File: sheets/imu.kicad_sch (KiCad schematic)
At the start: 11 parts, among them CN1 StemmaQT, CN2 StemmaQT, U2 BMP581, U5 ADXL375BCCZ-RL7, U7 ADXL345BCCZ-RL7

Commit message: added current rush limiting resistors to bmp581
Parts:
- added R24, R25: 10, symbol Device:R
- U5: footprint easyeda2kicad:LGA-14_L5.0-W3.0-P0.80-BL -> aerolotl_custom:LGA-14_L5.0-W3.0-P0.80-BL
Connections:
- net GND: now also CIO1.2, CS1.2, U5.11 (RESERVED), U7.11 (RESERVED_11)
- net VDD: now also U5.3 (RESERVED), U7.3 (RESERVED_3), R24.1, R25.1; no longer C32.1, C33.1, U2.1 (VDDIO), U2.10 (VDD)
- net ADXL345.INT: now reaches U7.8 (INT1)
- net ADXL375.INT: now reaches U5.8 (INT1)
- new net: C32.1, R24.2, U2.10 (VDD)
- new net: C33.1, R25.2, U2.1 (VDDIO)
- no-connect marks 2 -> 4
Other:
- note added: "ADXL375"
- note added: "BNO085 uses the Adafruit breakout board (no chip in stock in JLCPCB) via a StemmaQT connector"
- note added: "NEOM9N uses sparkfun breakout board"
- note added: "R = 10Ohm for inrush current limiting + LPF for stable voltage source"
- note removed: "TODO list: - Add the stemma qt adapter for the BNO085 -> DONE (Only labeled; from FlyPho) - Add the BMP581 connections (SPI 4-wire) -> DONE (from datasheet) - Add UART to GPS Neo m9n module -> WAITING (possible ITAR restriction) - Add ADXL345 and ADXL 375 via SPI -> IN PROGRESS"
- moved on the sheet: C32, C33, CIO1, CS1, U2, U5

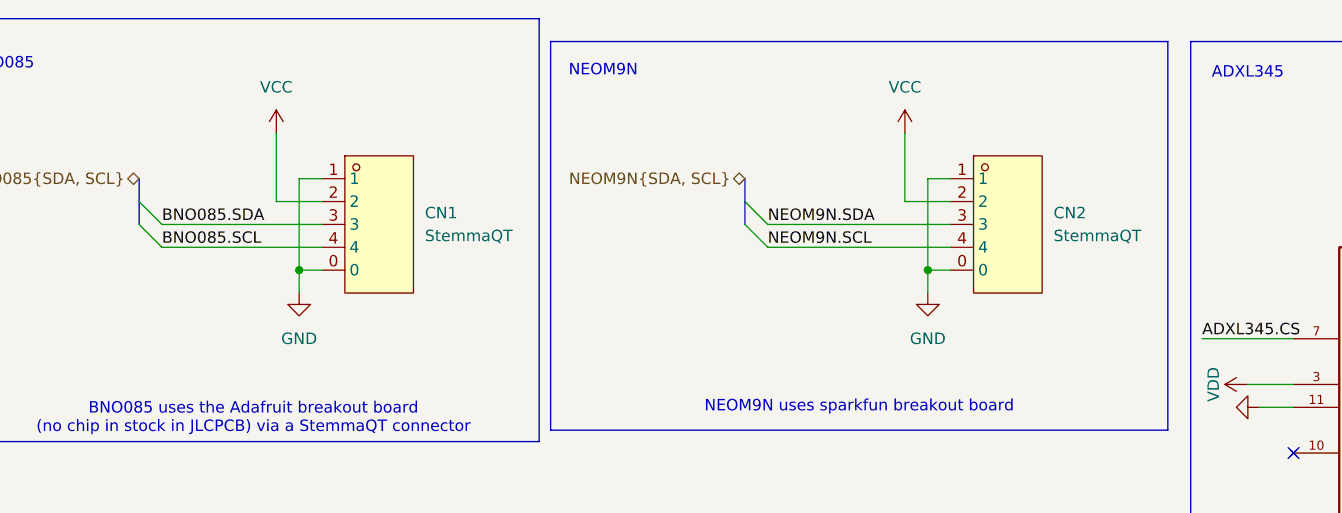
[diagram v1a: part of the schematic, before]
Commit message: Added NEOM9N breakout symbol
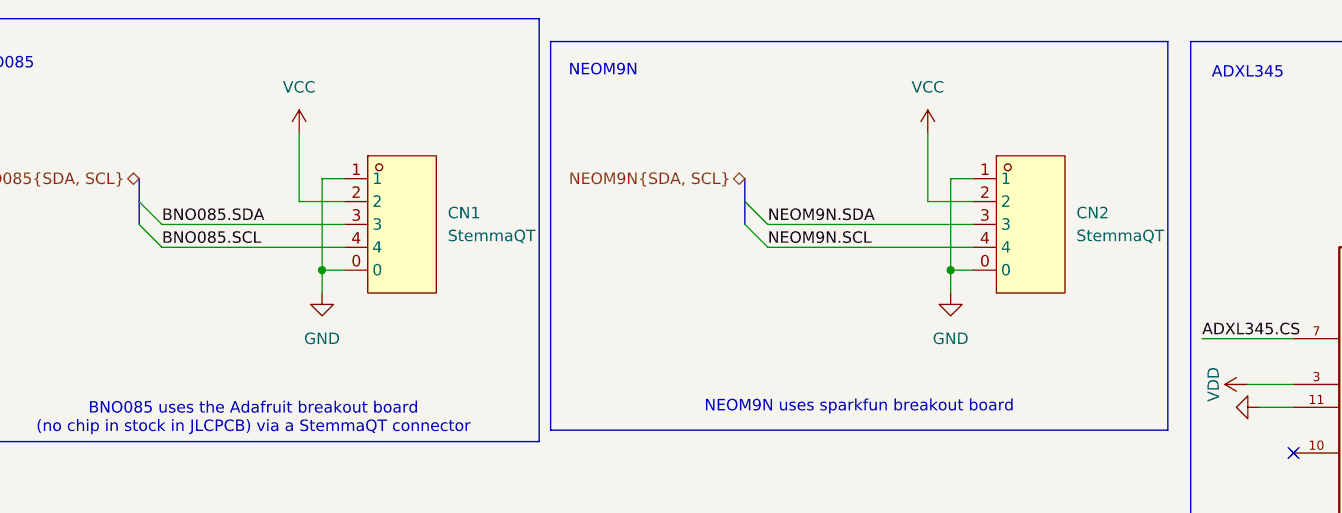
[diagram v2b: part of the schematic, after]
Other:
- moved on the sheet: CN1, CN2
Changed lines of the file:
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@@
 	)
 	(junction
-		(at 125.73 44.45)
+		(at 128.27 44.45)
 		(diameter 0)
 		(color 0 0 0 0)
@@
 	)
 	(junction
-		(at 55.88 44.45)
+		(at 58.42 44.45)
 		(diameter 0)
 		(color 0 0 0 0)
@@
 	(wire
 		(pts
-			(xy 123.19 29.21) (xy 123.19 36.83)
+			(xy 125.73 29.21) (xy 125.73 36.83)
 		)
 		(stroke
@@
 	(wire
 		(pts
-			(xy 58.42 34.29) (xy 55.88 34.29)
+			(xy 60.96 34.29) (xy 58.42 34.29)
 		)
 		(stroke
@@
 	(wire
 		(pts
-			(xy 125.73 44.45) (xy 125.73 46.99)
+			(xy 128.27 44.45) (xy 128.27 46.99)
 		)
 		(stroke
@@
 	(wire
 		(pts
-			(xy 53.34 36.83) (xy 58.42 36.83)
+			(xy 55.88 36.83) (xy 60.96 36.83)
 		)
 		(stroke
@@
 	(wire
 		(pts
-			(xy 40.64 41.91) (xy 58.42 41.91)
+			(xy 40.64 41.91) (xy 60.96 41.91)
 		)
 		(stroke
@@
 	(wire
 		(pts
-			(xy 125.73 34.29) (xy 125.73 44.45)
+			(xy 128.27 34.29) (xy 128.27 44.45)
 		)
 		(stroke
@@
 	(wire
 		(pts
-			(xy 53.34 29.21) (xy 53.34 36.83)
+			(xy 55.88 29.21) (xy 55.88 36.83)
 		)
 		(stroke
@@
 	(wire
 		(pts
-			(xy 128.27 34.29) (xy 125.73 34.29)
+			(xy 130.81 34.29) (xy 128.27 34.29)
 		)
 		(stroke
@@
 	(wire
 		(pts
-			(xy 55.88 44.45) (xy 58.42 44.45)
+			(xy 58.42 44.45) (xy 60.96 44.45)
 		)
 		(stroke
@@
 	(wire
 		(pts
-			(xy 125.73 44.45) (xy 128.27 44.45)
+			(xy 128.27 44.45) (xy 130.81 44.45)
 		)
 		(stroke
@@
 	(wire
 		(pts
-			(xy 107.95 41.91) (xy 128.27 41.91)
+			(xy 107.95 41.91) (xy 130.81 41.91)
 		)
 		(stroke
@@
 	(wire
 		(pts
-			(xy 123.19 36.83) (xy 128.27 36.83)
+			(xy 125.73 36.83) (xy 130.81 36.83)
 		)
 		(stroke
@@
 	(wire
 		(pts
-			(xy 55.88 34.29) (xy 55.88 44.45)
+			(xy 58.42 34.29) (xy 58.42 44.45)
 		)
 		(stroke
@@
 	(wire
 		(pts
-			(xy 40.64 39.37) (xy 58.42 39.37)
+			(xy 40.64 39.37) (xy 60.96 39.37)
 		)
 		(stroke
@@
 	(wire
 		(pts
-			(xy 107.95 39.37) (xy 128.27 39.37)
+			(xy 107.95 39.37) (xy 130.81 39.37)
 		)
 		(stroke
@@
 	(wire
 		(pts
-			(xy 55.88 44.45) (xy 55.88 46.99)
+			(xy 58.42 44.45) (xy 58.42 46.99)
 		)
 		(stroke
@@
 	(symbol
 		(lib_id "power:VCC")
-		(at 123.19 29.21 0)
+		(at 125.73 29.21 0)
 		(unit 1)
 		(exclude_from_sim no)
@@
 		(fields_autoplaced yes)
 		(property "Reference" "#PWR053"
-			(at 123.19 33.02 0)
+			(at 125.73 33.02 0)
 			(effects
 				(font
@@
 		)
 		(property "Value" "VCC"
-			(at 123.19 24.13 0)
+			(at 125.73 24.13 0)
 			(effects
 				(font
@@
 		)
 		(property "Footprint" ""
-			(at 123.19 29.21 0)
+			(at 125.73 29.21 0)
 			(effects
 				(font
@@
 		)
 		(property "Datasheet" ""
-			(at 123.19 29.21 0)
+			(at 125.73 29.21 0)
 			(effects
 				(font
@@
 		)
 		(property "Description" "Power symbol creates a global label with name \"VCC\""
-			(at 123.19 29.21 0)
+			(at 125.73 29.21 0)
 			(effects
 				(font
@@
 	(symbol
 		(lib_id "power:GND")
-		(at 55.88 46.99 0)
+		(at 58.42 46.99 0)
 		(unit 1)
 		(exclude_from_sim no)
@@
 		(fields_autoplaced yes)
 		(property "Reference" "#PWR047"
-			(at 55.88 53.34 0)
+			(at 58.42 53.34 0)
 			(effects
 				(font
@@
 		)
 		(property "Value" "GND"
-			(at 55.88 52.07 0)
+			(at 58.42 52.07 0)
 			(effects
 				(font
@@
 		)
 		(property "Footprint" ""
-			(at 55.88 46.99 0)
+			(at 58.42 46.99 0)
 			(effects
 				(font
@@
 		)
 		(property "Datasheet" ""
-			(at 55.88 46.99 0)
+			(at 58.42 46.99 0)
 			(effects
 				(font
@@
 		)
 		(property "Description" "Power symbol creates a global label with name \"GND\" , ground"
-			(at 55.88 46.99 0)
+			(at 58.42 46.99 0)
 			(effects
 				(font
@@
 	(symbol
 		(lib_id "aerolotl_custom:StemmaQT")
-		(at 63.5 39.37 0)
+		(at 66.04 39.37 0)
 		(unit 1)
 		(exclude_from_sim no)
@@
 		(fields_autoplaced yes)
 		(property "Reference" "CN1"
-			(at 69.85 38.0999 0)
+			(at 72.39 38.0999 0)
 			(effects
 				(font
@@
 		)
 		(property "Value" "StemmaQT"
-			(at 69.85 40.6399 0)
+			(at 72.39 40.6399 0)
 			(effects
 				(font
@@
 		)
 		(property "Footprint" "aerolotl_custom:CONN-SMD_BM04B-SRSS-TB"
-			(at 63.5 52.07 0)
+			(at 66.04 52.07 0)
 			(effects
 				(font
@@
 		)
 		(property "Datasheet" "https://lcsc.com/product-detail/Others_JST-Sales-America__JST-Sales-America-BM04B-SRSS-TB-LF-SN_C160390.html"
-			(at 63.5 54.61 0)
+			(at 66.04 54.61 0)
 			(effects
 				(font
@@
 		)
 		(property "Description" ""
-			(at 63.5 39.37 0)
+			(at 66.04 39.37 0)
 			(effects
 				(font
@@
 		)
 		(property "LCSC Part" "C160390"
-			(at 63.5 57.15 0)
+			(at 66.04 57.15 0)
 			(effects
 				(font
@@
 	(symbol
 		(lib_id "power:GND")
-		(at 125.73 46.99 0)
+		(at 128.27 46.99 0)
 		(unit 1)
 		(exclude_from_sim no)
@@
 		(fields_autoplaced yes)
 		(property "Reference" "#PWR054"
-			(at 125.73 53.34 0)
+			(at 128.27 53.34 0)
 			(effects
 				(font
@@
 		)
 		(property "Value" "GND"
-			(at 125.73 52.07 0)
+			(at 128.27 52.07 0)
 			(effects
 				(font
@@
 		)
 		(property "Footprint" ""
-			(at 125.73 46.99 0)
+			(at 128.27 46.99 0)
 			(effects
 				(font
@@
 		)
 		(property "Datasheet" ""
-			(at 125.73 46.99 0)
+			(at 128.27 46.99 0)
 			(effects
 				(font
@@
 		)
 		(property "Description" "Power symbol creates a global label with name \"GND\" , ground"
-			(at 125.73 46.99 0)
+			(at 128.27 46.99 0)
 			(effects
 				(font
@@
 	(symbol
 		(lib_id "aerolotl_custom:StemmaQT")
-		(at 133.35 39.37 0)
+		(at 135.89 39.37 0)
 		(unit 1)
 		(exclude_from_sim no)
@@
 		(fields_autoplaced yes)
 		(property "Reference" "CN2"
-			(at 139.7 38.0999 0)
+			(at 142.24 38.0999 0)
 			(effects
 				(font
@@
 		)
 		(property "Value" "StemmaQT"
-			(at 139.7 40.6399 0)
+			(at 142.24 40.6399 0)
 			(effects
 				(font
@@
 		)
 		(property "Footprint" "aerolotl_custom:CONN-SMD_BM04B-SRSS-TB"
-			(at 133.35 52.07 0)
+			(at 135.89 52.07 0)
 			(effects
 				(font
@@
 		)
 		(property "Datasheet" "https://lcsc.com/product-detail/Others_JST-Sales-America__JST-Sales-America-BM04B-SRSS-TB-LF-SN_C160390.html"
-			(at 133.35 54.61 0)
+			(at 135.89 54.61 0)
 			(effects
 				(font
@@
 		)
 		(property "Description" ""
-			(at 133.35 39.37 0)
+			(at 135.89 39.37 0)
 			(effects
 				(font
@@
 		)
 		(property "LCSC Part" "C160390"
-			(at 133.35 57.15 0)
+			(at 135.89 57.15 0)
 			(effects
 				(font
@@
 	(symbol
 		(lib_id "power:VCC")
-		(at 53.34 29.21 0)
+		(at 55.88 29.21 0)
 		(unit 1)
 		(exclude_from_sim no)
@@
 		(fields_autoplaced yes)
 		(property "Reference" "#PWR034"
-			(at 53.34 33.02 0)
+			(at 55.88 33.02 0)
 			(effects
 				(font
@@
 		)
 		(property "Value" "VCC"
-			(at 53.34 24.13 0)
+			(at 55.88 24.13 0)
 			(effects
 				(font
@@
 		)
 		(property "Footprint" ""
-			(at 53.34 29.21 0)
+			(at 55.88 29.21 0)
 			(effects
 				(font
@@
 		)
 		(property "Datasheet" ""
-			(at 53.34 29.21 0)
+			(at 55.88 29.21 0)
 			(effects
 				(font
@@
 		)
 		(property "Description" "Power symbol creates a global label with name \"VCC\""
-			(at 53.34 29.21 0)
+			(at 55.88 29.21 0)
 			(effects
 				(font

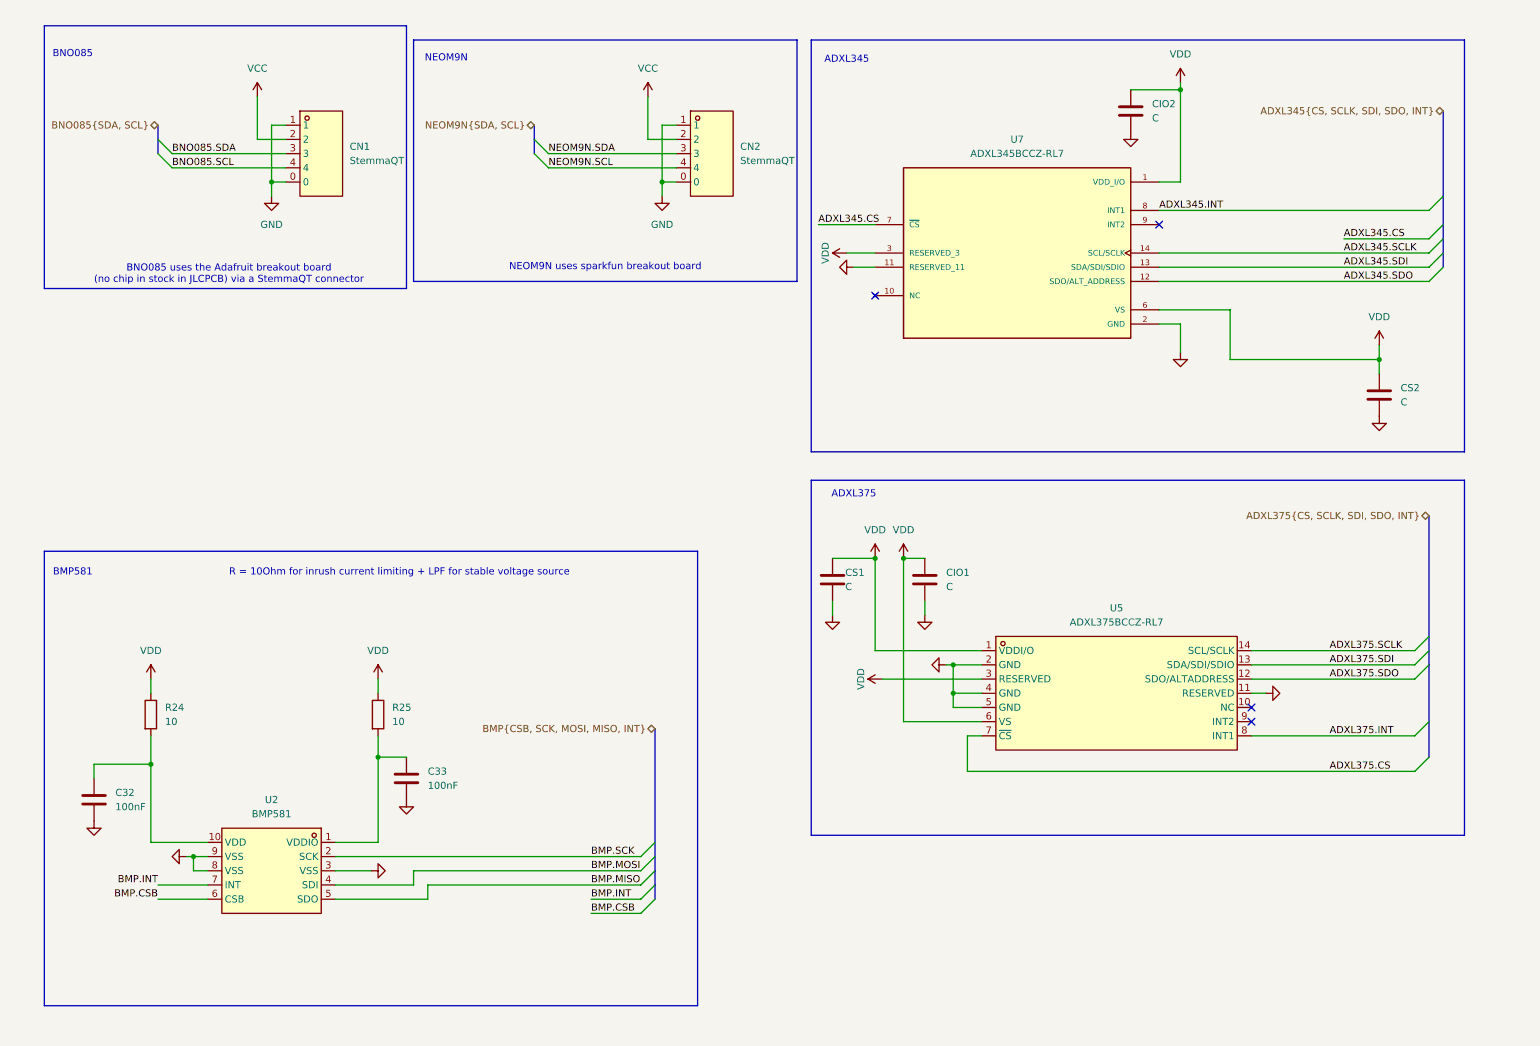
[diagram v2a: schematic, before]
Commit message: Wired NEOM9N breakout
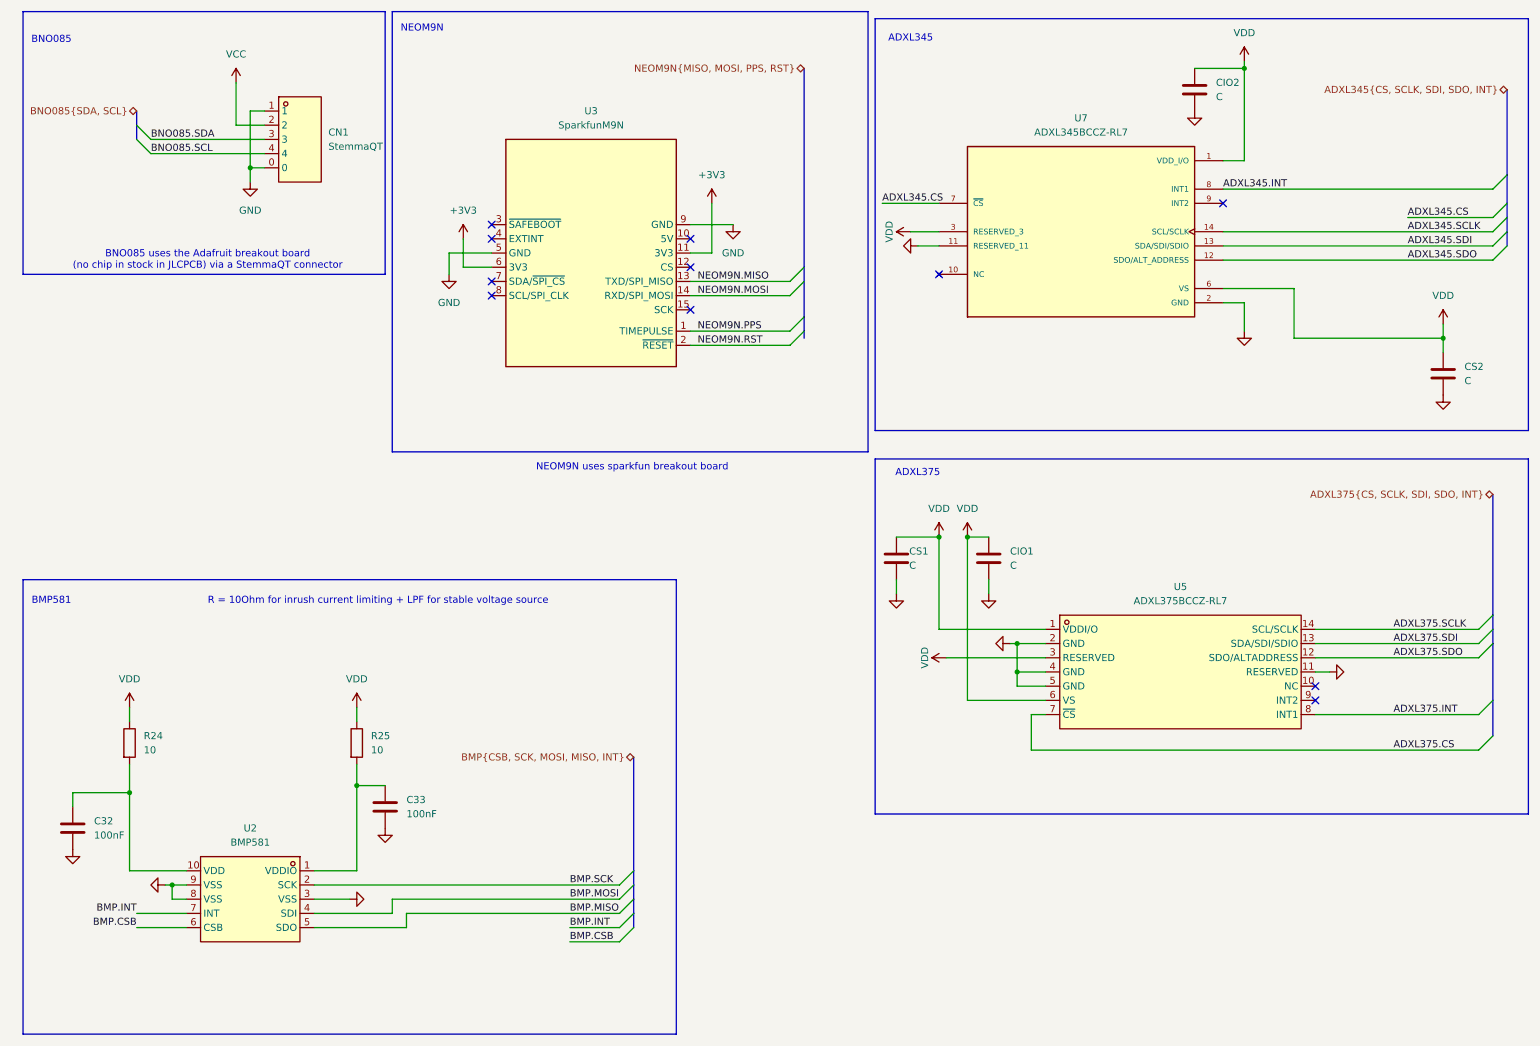
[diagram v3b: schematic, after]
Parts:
- removed CN2: StemmaQT, aerolotl_custom:CONN-SMD_BM04B-SRSS-TB, symbol aerolotl_custom:StemmaQT
- added U3: SparkfunM9N, RF_GPS:ublox_NEO, symbol aerolotl_custom:SparkfunM9N
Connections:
- net GND: now also U3.5 (GND), U3.9 (GND)
- new net +3V3: U3.11 (3V3), U3.6 (3V3)
- new net NEOM9N.MISO: U3.13 (TXD/SPI_MISO)
- new net NEOM9N.MOSI: U3.14 (RXD/SPI_MOSI)
- new net NEOM9N.PPS: U3.1 (TIMEPULSE)
- new net NEOM9N.RST: U3.2 (~{RESET})
- no-connect marks 4 -> 11
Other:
- moved on the sheet: C32, C33, CIO1, CIO2, CN1, CS1, CS2, R24, R25, U2, U5, U7

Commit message: Fixed up power, added remaining to do
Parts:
- U3: footprint RF_GPS:ublox_NEO -> aerolotl_custom:SparkfunM9N
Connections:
- net NEOM9N.MISO renamed NEOM9N.TX
- net NEOM9N.MOSI renamed NEOM9N.RX
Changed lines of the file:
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@@
 		)
 	)
-	(label "NEOM9N.MOSI"
+	(label "NEOM9N.RX"
 		(at 134.62 64.77 0)
 		(effects
@@
 		)
 	)
-	(label "NEOM9N.MISO"
+	(label "NEOM9N.TX"
 		(at 134.62 62.23 0)
 		(effects
@@
 		)
 	)
-	(hierarchical_label "NEOM9N{MISO, MOSI, PPS, RST}"
+	(hierarchical_label "NEOM9N{TX, RX, PPS, RST}"
 		(shape bidirectional)
 		(at 153.67 24.13 180)
@@
 			)
 		)
-		(property "Footprint" "RF_GPS:ublox_NEO"
+		(property "Footprint" "aerolotl_custom:SparkfunM9N"
 			(at 125.73 19.812 0)
 			(effects
